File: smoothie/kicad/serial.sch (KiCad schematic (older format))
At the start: 7 parts, among them IC3 AMS1117-3.3, J9 CHILLER SERIAL, U1 MAX485

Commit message: More work on PCB.
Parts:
- added C10, C11: 100u, SMD_Packages:SMD-1206_Pol, symbol CP
- added D1: D, LEDs:LED_0603, symbol D
- added J10: TO_J7, Connectors:PINHEAD1-6, symbol CONN_01X06
- added J11: 24V PWR, Connectors_JST:JST_PH_B2B-PH-K_02x2.00mm_Straight, symbol CONN_01X02
- added J12: LED LIGHTING, Connectors_JST:JST_PH_B2B-PH-K_02x2.00mm_Straight, symbol CONN_01X02
- added J13: AIR VALVE, Connectors_JST:JST_PH_B2B-PH-K_02x2.00mm_Straight, symbol CONN_01X02
- added J14: AIMING LASER, Connectors_JST:JST_PH_B2B-PH-K_02x2.00mm_Straight, symbol CONN_01X02
- added J5: POWEROFF, Connectors_JST:JST_PH_B3B-PH-K_03x2.00mm_Straight, symbol CONN_01X03
- added Q1: ZXMN4A06, TO_SOT_Packages_SMD:SOT-223-3Lead_TabPin2, symbol Q_NMOS_GDS
- added R11: 10K, Resistors_SMD:R_0603, symbol R
- added R12: 22R, Resistors_SMD:R_0603, symbol R
- added U2: DSN-MINI-360, dsn-mini-360:DSN-MINI-360, symbol DSN-MINI-360
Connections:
- net +5V: now also J14.1 (P1), J5.3 (P3)
- net GND: now also C10.2, C11.2, J11.2 (P2), J12.2 (P2), J14.2 (P2), J5.1 (P1), Q1.3 (S), R11.2, U2.IN-, U2.OUT-
- new net: J10.4 (P4), J5.2 (P2)
- new net: J10.6 (P6), R11.1, R12.2
- new net: C10.1, J11.1 (P1), U2.IN+
- new net: C11.1, D1.1 (K), J12.1 (P1), J13.1 (P1), U2.OUT+
- new net: D1.2 (A), J13.2 (P2), Q1.2 (D)
- new net: Q1.1 (G), R12.1
- no-connect marks 0 -> 4
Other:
- note added: "1: +5V\n2: NC\n3: GND\n4: 0.17\n5: 0.16\n6: 0.15"
- note removed: "!!level conversoin"

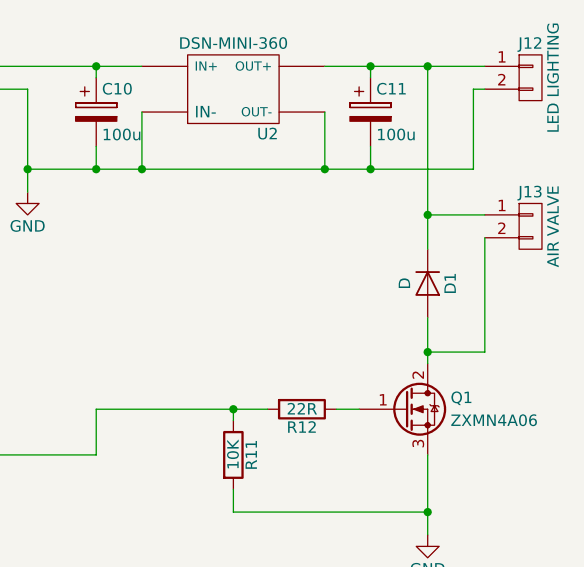
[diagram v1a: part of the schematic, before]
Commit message: Finish routing.
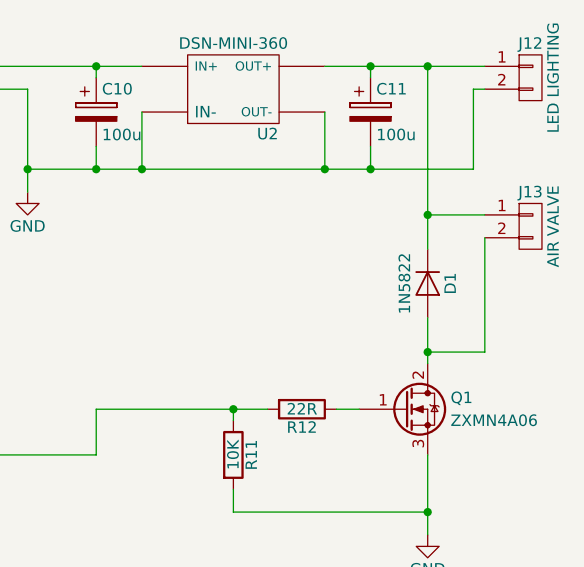
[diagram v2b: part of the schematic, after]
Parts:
- D1: value D -> 1N5822; footprint LEDs:LED_0603 -> Diodes_SMD:D_SMC_Standard
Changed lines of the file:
@@
 P 7150 4450
 F 0 "D1" H 7150 4550 50  0000 C CNN
-F 1 "D" H 7150 4350 50  0000 C CNN
-F 2 "LEDs:LED_0603" H 7150 4450 50  0001 C CNN
+F 1 "1N5822" H 7150 4350 50  0000 C CNN
+F 2 "Diodes_SMD:D_SMC_Standard" H 7150 4450 50  0001 C CNN
 F 3 "" H 7150 4450 50  0001 C CNN
 	1    7150 4450

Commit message: Change D1 to SS34.
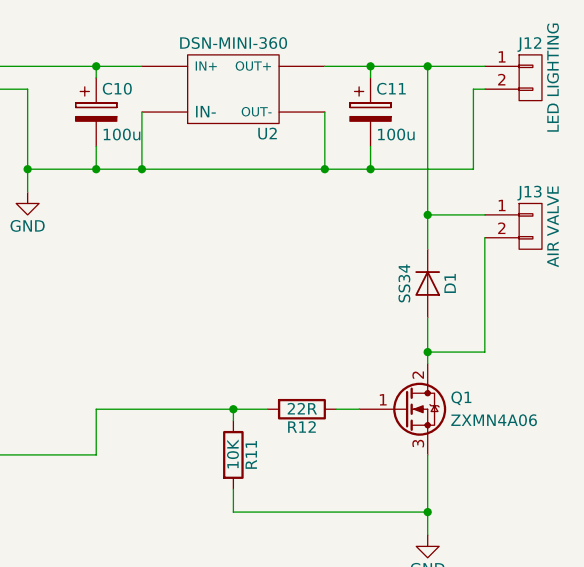
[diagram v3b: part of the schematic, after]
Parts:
- D1: value 1N5822 -> SS34; footprint Diodes_SMD:D_SMC_Standard -> Diodes_SMD:D_SMA_Standard
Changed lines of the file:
@@
 P 7150 4450
 F 0 "D1" H 7150 4550 50  0000 C CNN
-F 1 "1N5822" H 7150 4350 50  0000 C CNN
-F 2 "Diodes_SMD:D_SMC_Standard" H 7150 4450 50  0001 C CNN
+F 1 "SS34" H 7150 4350 50  0000 C CNN
+F 2 "Diodes_SMD:D_SMA_Standard" H 7150 4450 50  0001 C CNN
 F 3 "" H 7150 4450 50  0001 C CNN
 	1    7150 4450

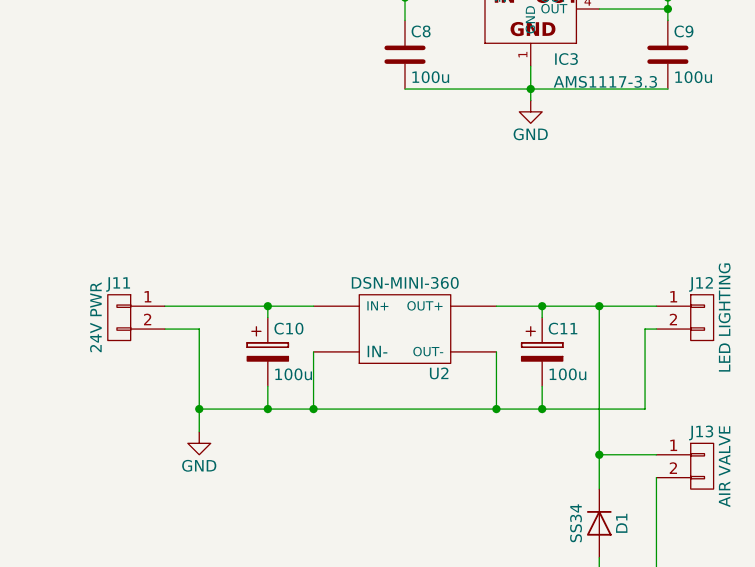
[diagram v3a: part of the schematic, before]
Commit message: Fix door switch high/low.
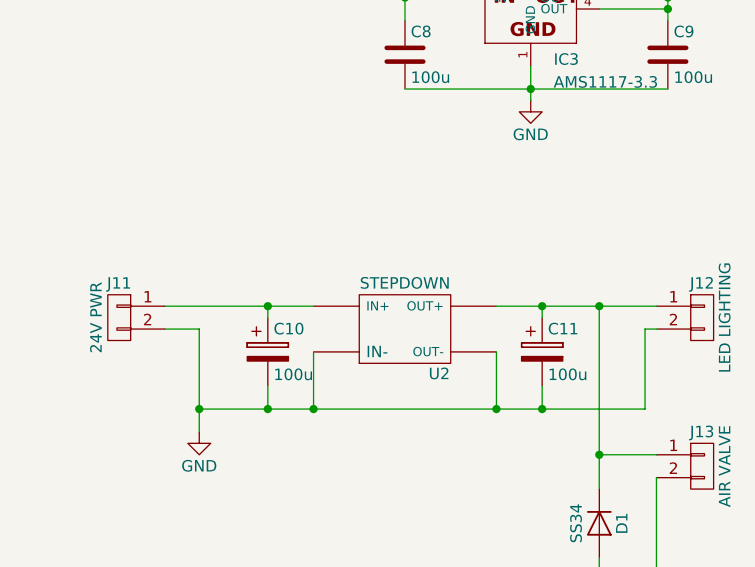
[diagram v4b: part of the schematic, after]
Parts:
- U2: value DSN-MINI-360 -> STEPDOWN
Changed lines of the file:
@@
 P 6300 3600
 F 0 "U2" H 6450 3404 50  0000 C CNN
-F 1 "DSN-MINI-360" H 6300 3800 50  0000 C CNN
+F 1 "STEPDOWN" H 6300 3800 50  0000 C CNN
 F 2 "dsn-mini-360:DSN-MINI-360" H 6300 3600 50  0001 C CNN
 F 3 "" H 6300 3600 50  0001 C CNN
